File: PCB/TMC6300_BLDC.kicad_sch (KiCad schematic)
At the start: 14 parts, among them J2 Conn_01x03, U4 TMC6300-LA-T_C5274455

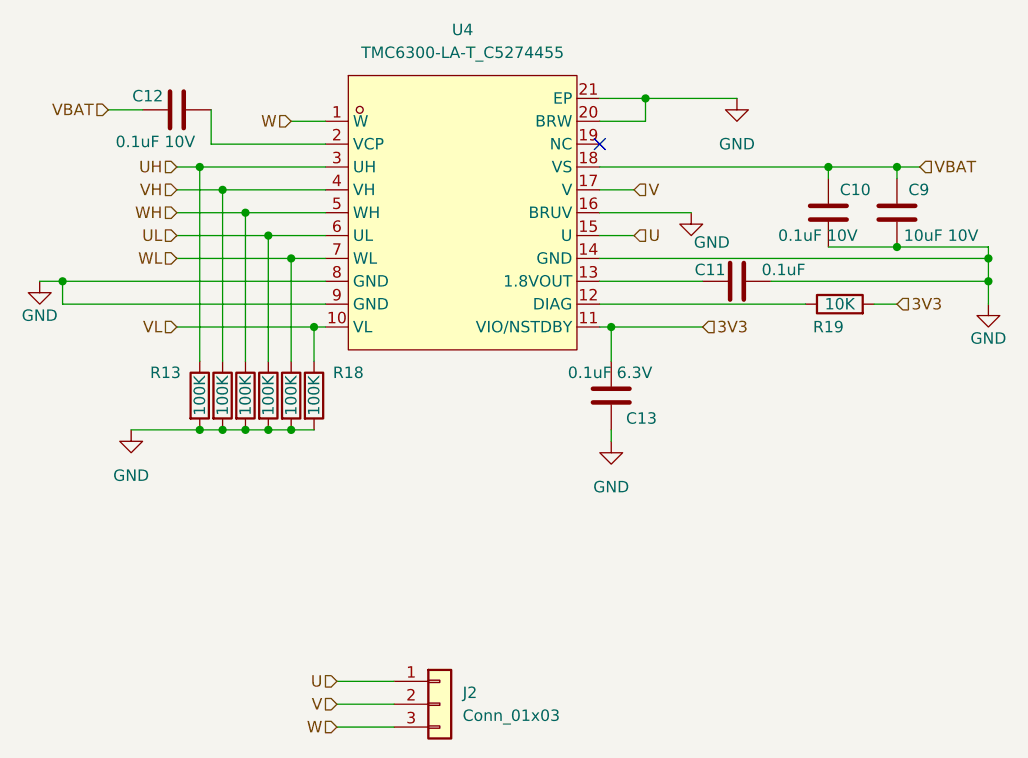
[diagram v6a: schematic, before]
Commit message: PCB schematic checked - ready to trace
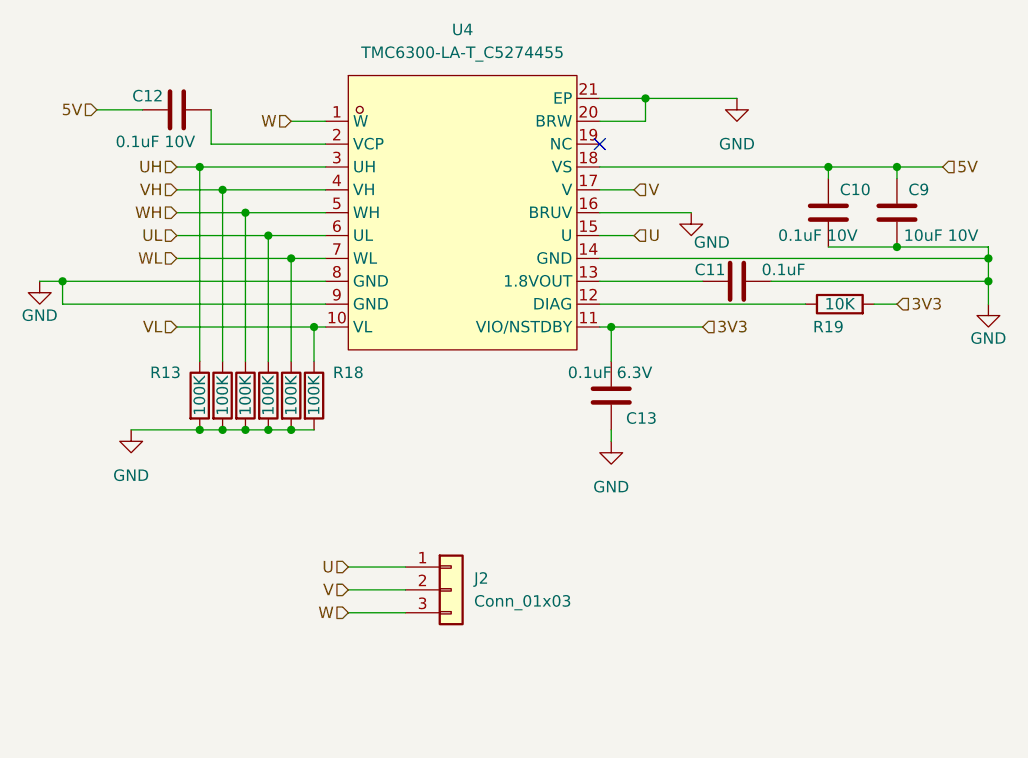
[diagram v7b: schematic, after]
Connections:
- net VBAT renamed 5V
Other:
- moved on the sheet: J2
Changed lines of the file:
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@@
 	(wire
 		(pts
-			(xy 119.38 154.94) (xy 125.73 154.94)
-		)
-		(stroke
-			(width 0)
-			(type default)
-		)
-	)
-	(wire
-		(pts
-			(xy 181.61 97.79) (xy 184.15 97.79)
+			(xy 120.65 142.24) (xy 127 142.24)
+		)
+		(stroke
+			(width 0)
+			(type default)
+		)
+	)
+	(wire
+		(pts
+			(xy 181.61 97.79) (xy 186.69 97.79)
+		)
+		(stroke
+			(width 0)
+			(type default)
+		)
+	)
+	(wire
+		(pts
+			(xy 92.71 91.44) (xy 97.79 91.44)
 		)
 		(stroke
@@
 	(wire
 		(pts
-			(xy 119.38 160.02) (xy 125.73 160.02)
+			(xy 120.65 147.32) (xy 127 147.32)
 		)
 		(stroke
@@
 	(wire
 		(pts
-			(xy 119.38 157.48) (xy 125.73 157.48)
+			(xy 120.65 144.78) (xy 127 144.78)
 		)
 		(stroke
@@
 		(pts
 			(xy 148.59 97.79) (xy 173.99 97.79)
-		)
-		(stroke
-			(width 0)
-			(type default)
-		)
-	)
-	(wire
-		(pts
-			(xy 93.98 91.44) (xy 97.79 91.44)
 		)
 		(stroke
@@
 		)
 	)
-	(hierarchical_label "VBAT"
-		(shape input)
-		(at 93.98 91.44 180)
-		(effects
-			(font
-				(size 1.27 1.27)
-			)
-			(justify right)
-		)
-	)
 	(hierarchical_label "WH"
 		(shape input)
@@
 	(hierarchical_label "V"
 		(shape input)
-		(at 119.38 157.48 180)
+		(at 120.65 144.78 180)
 		(effects
 			(font
@@
 		)
 	)
+	(hierarchical_label "5V"
+		(shape input)
+		(at 186.69 97.79 0)
+		(effects
+			(font
+				(size 1.27 1.27)
+			)
+			(justify left)
+		)
+	)
+	(hierarchical_label "5V"
+		(shape input)
+		(at 92.71 91.44 180)
+		(effects
+			(font
+				(size 1.27 1.27)
+			)
+			(justify right)
+		)
+	)
 	(hierarchical_label "U"
 		(shape input)
@@
 	(hierarchical_label "W"
 		(shape input)
-		(at 119.38 160.02 180)
+		(at 120.65 147.32 180)
 		(effects
 			(font
@@
 		)
 	)
-	(hierarchical_label "VBAT"
-		(shape input)
-		(at 184.15 97.79 0)
-		(effects
-			(font
-				(size 1.27 1.27)
-			)
-			(justify left)
-		)
-	)
 	(hierarchical_label "U"
 		(shape input)
-		(at 119.38 154.94 180)
+		(at 120.65 142.24 180)
 		(effects
 			(font
@@
 	(symbol
 		(lib_id "Connector_Generic:Conn_01x03")
-		(at 130.81 157.48 0)
+		(at 132.08 144.78 0)
 		(unit 1)
 		(exclude_from_sim no)
@@
 		(fields_autoplaced yes)
 		(property "Reference" "J2"
-			(at 133.35 156.2099 0)
+			(at 134.62 143.5099 0)
 			(effects
 				(font
@@
 		)
 		(property "Value" "Conn_01x03"
-			(at 133.35 158.7499 0)
+			(at 134.62 146.0499 0)
 			(effects
 				(font
@@
 		)
 		(property "Footprint" "Connector_PinHeader_2.54mm:PinHeader_1x03_P2.54mm_Horizontal"
-			(at 130.81 157.48 0)
+			(at 132.08 144.78 0)
 			(effects
 				(font
@@
 		)
 		(property "Datasheet" "~"
-			(at 130.81 157.48 0)
+			(at 132.08 144.78 0)
 			(effects
 				(font
@@
 		)
 		(property "Description" "Generic connector, single row, 01x03, script generated (kicad-library-utils/schlib/autogen/connector/)"
-			(at 130.81 157.48 0)
-			(effects
-				(font
+			(at 132.08 144.78 0)
+			(effects
+				(font

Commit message: final checks for PCB, nearly ready to order v1
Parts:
- C9: value 10uF 10V -> 47uF; footprint Capacitor_SMD:C_0402_1005Metric -> Capacitor_SMD:C_0805_2012Metric
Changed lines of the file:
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@@
 			)
 		)
-		(property "Value" "10uF 10V"
+		(property "Value" "47uF"
 			(at 182.372 105.41 0)
 			(effects
@@
 			)
 		)
-		(property "Footprint" "Capacitor_SMD:C_0402_1005Metric"
+		(property "Footprint" "Capacitor_SMD:C_0805_2012Metric"
 			(at 182.5752 106.68 0)
 			(effects
